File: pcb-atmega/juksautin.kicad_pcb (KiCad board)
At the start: 2 copper layers, 65 x 35 mm, 29 parts, among them J1 Screw_Terminal_01x09, J2 Power out, J3 USB_C_Receptacle_USB2.0, J4 TagConnect, J5 EXTRA, J6 AREF_OUT, U1 SP3485EN, U2 SRV05-4, U3 R-78E5.0-0.5, U4 ATmega32U4-AU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

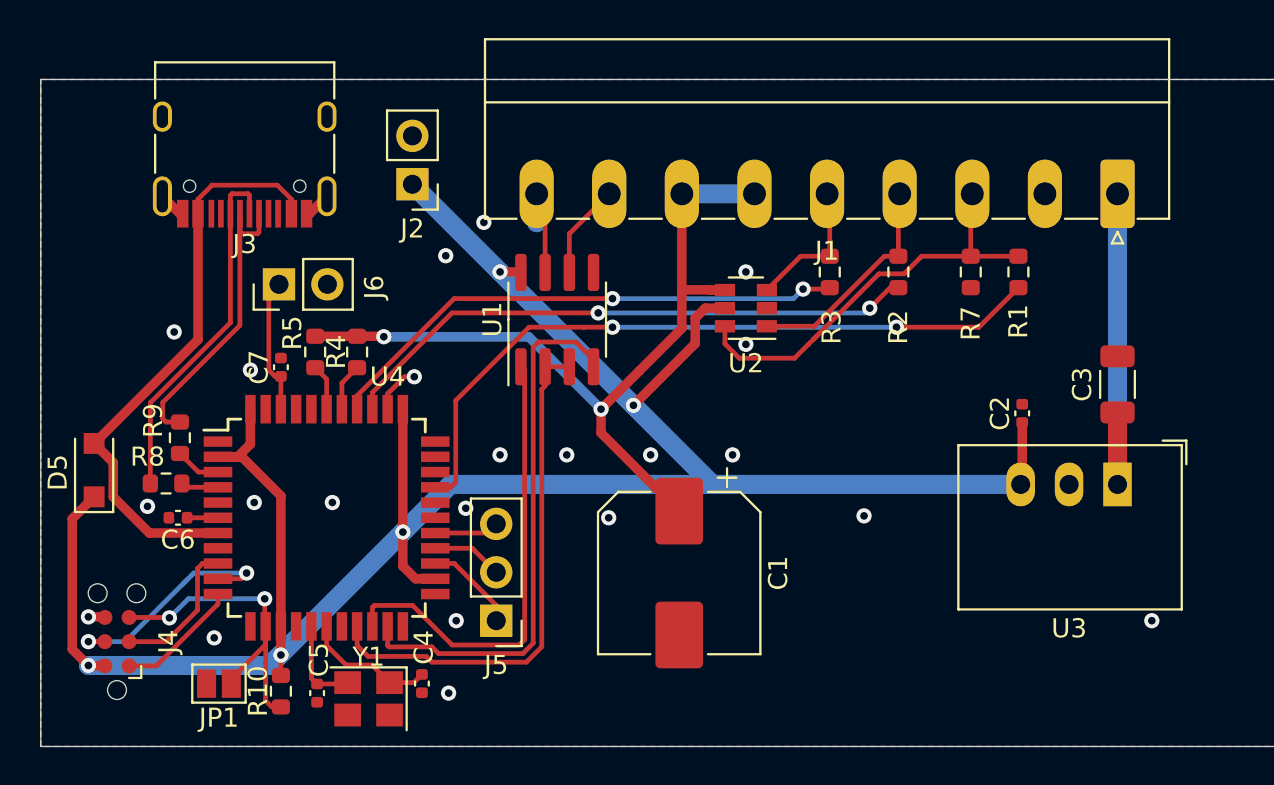
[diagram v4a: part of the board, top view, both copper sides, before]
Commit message: Atmega328 based pcb layed out
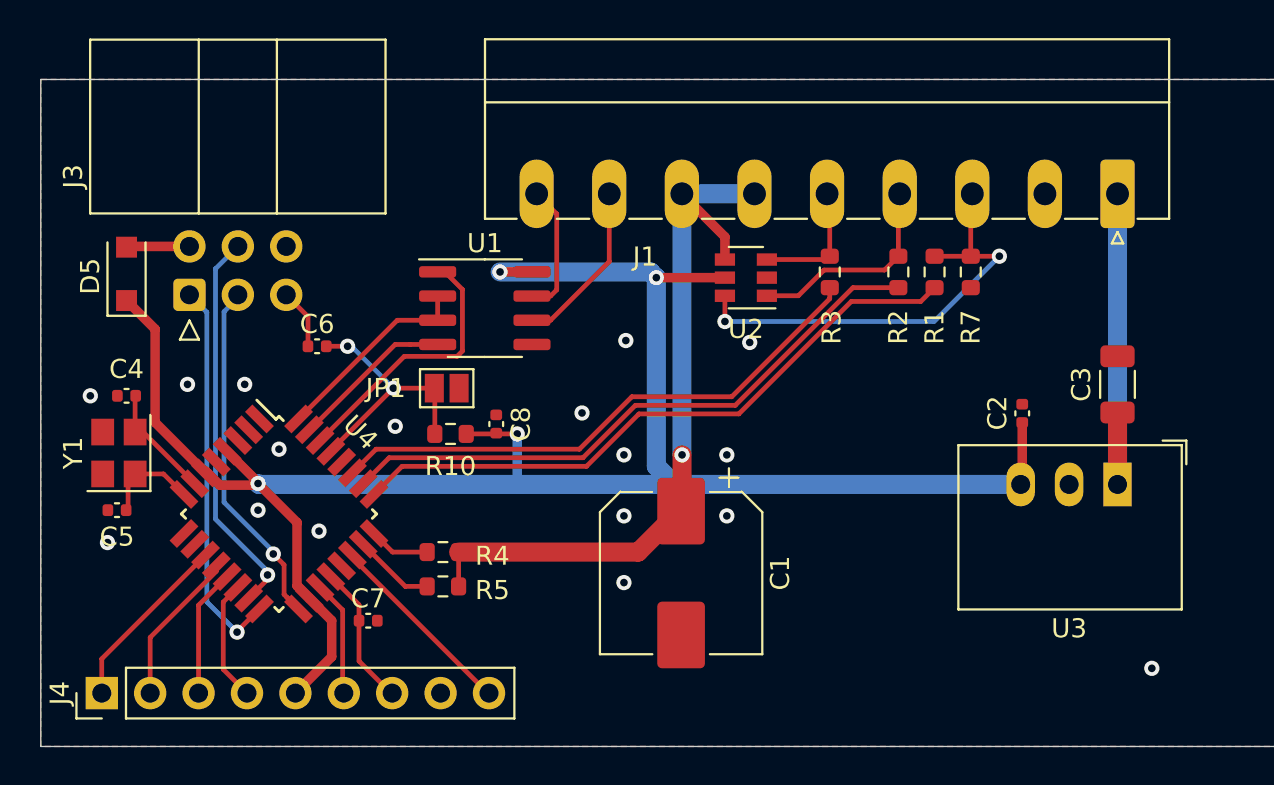
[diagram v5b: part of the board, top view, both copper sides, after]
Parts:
- removed J2: Power out, Connector_PinHeader_2.54mm:PinHeader_1x02_P2.54mm_Vertical
- removed J5: EXTRA, Connector_PinHeader_2.54mm:PinHeader_1x03_P2.54mm_Vertical
- removed J6: AREF_OUT, Connector_PinHeader_2.54mm:PinHeader_1x02_P2.54mm_Vertical
- removed R8, R9: 22, Resistor_SMD:R_0603_1608Metric
- added C8: 100n, Capacitor_SMD:C_0402_1005Metric, F.Cu at (133.9, 83.1)
- C6: value 1u -> 100n
- J3: value USB_C_Receptacle_USB2.0 -> AVR-ISP-6; footprint Connector_USB:USB_C_Receptacle_HRO_TYPE-C-31-M-12 -> Connector_IDC:IDC-Header_2x03_P2.54mm_Horizontal
- J4: value TagConnect -> Conn_01x09; footprint Connector:Tag-Connect_TC2030-IDC-NL_2x03_P1.27mm_Vertical -> Connector_PinHeader_2.54mm:PinHeader_1x09_P2.54mm_Vertical
- R10: value 20k -> 10k
- U4: value ATmega32U4-AU -> ATmega328P-AU; footprint Package_QFP:TQFP-44_10x10mm_P0.8mm -> Package_QFP:TQFP-32_7x7mm_P0.8mm
- moved C4 21.6 mm to (114.5, 81.6), turned to 180 degrees
- moved JP1 19.6 mm to (131.3, 81.2), turned to 0 degrees
- moved Y1 18.4 mm to (114.1, 84.6), turned to 90 degrees
- moved R10 16.2 mm to (131.5, 83.6), turned to 180 degrees
- moved C5 14.2 mm to (114.0, 87.6), turned to 180 degrees
- moved C7 14.1 mm to (127.2, 93.4), turned to 0 degrees
- moved R5 14.0 mm to (131.1, 91.6), turned to 0 degrees
- moved C6 11.6 mm to (124.5, 79.0), turned to 0 degrees
- moved R4 11.4 mm to (131.1, 89.8), turned to 0 degrees
- moved D5 10.4 mm to (114.5, 75.2)
- moved J3 8.79 mm to (117.8, 76.3), turned to 90 degrees
- moved R1 4.40 mm to (156.9, 75.1)
- moved U1 3.85 mm to (133.3, 77.0), turned to 0 degrees
- moved J4 2.82 mm to (113.2, 97.2)
- moved U4 2.51 mm to (122.5, 87.8), turned to 315 degrees
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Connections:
- C6 pad 1: Net-(C6-Pad1) -> /RESET_IN
- C6 pad 2: GND -> /RESET
- J4 pad 1: /MISO -> /INO_D7
- J4 pad 2: VCC -> /INO_D8
- J4 pad 3: /SCK -> /INO_D9
- J4 pad 4: /MOSI -> /INO_D10
- J4 pad 5: /RESET -> VCC
- J4 pad 6: GND -> /INO_A6
- U4 pad 10: /MOSI -> (no net)
- U4 pad 11: /MISO -> /INO_D7
- U4 pad 12: (no net) -> /INO_D8
- U4 pad 13: /RESET -> /INO_D9
- U4 pad 14: VCC -> /INO_D10
- U4 pad 15: GND -> /MOSI
- U4 pad 16: Net-(C5-Pad1) -> /MISO
- U4 pad 17: Net-(C4-Pad1) -> /SCK
- U4 pad 18: (no net) -> VCC
- U4 pad 19: /TX_EN -> /INO_A6
- U4 pad 2: VCC -> (no net)
- U4 pad 20: /RX -> /AREF
- U4 pad 21: /TX -> GND
- U4 pad 22: (no net) -> /INO_A7
- U4 pad 23: GND -> /FB
- U4 pad 24: VCC -> /DRIVE
- U4 pad 25: Net-(J5-Pad1) -> /PUMPFAIL_M
- U4 pad 26: Net-(J5-Pad2) -> /IO1_M
- U4 pad 27: Net-(J5-Pad3) -> /IO2_M
- U4 pad 29: (no net) -> /RESET
- U4 pad 3: /DM -> GND
- U4 pad 30: /PUMPFAIL_M -> /RX
- U4 pad 31: (no net) -> /TX
- U4 pad 32: (no net) -> /TX_EN
- U4 pad 4: /DP -> VCC
- U4 pad 6: Net-(C6-Pad1) -> VCC
- U4 pad 7: /VBUS -> Net-(C4-Pad1)
- U4 pad 8: (no net) -> Net-(C5-Pad1)
- U4 pad 9: /SCK -> (no net)
- Y1 pad 1: Net-(C4-Pad1) -> Net-(C5-Pad1)
- Y1 pad 2: Net-(C5-Pad1) -> Net-(C4-Pad1)
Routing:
- net VCC: track 141.8 -> 103.8 mm, vias 5 -> 4
- net /VBUS: track 30.8 -> 3.46 mm
- net /TX: track 28.6 -> 8.59 mm
- net Net-(J3-PadA6): track 18.9 -> 0.00 mm
- net /TX_EN: track 27.4 -> 10.7 mm
- net Net-(J3-PadA7): track 16.4 -> 0.00 mm
- net /MISO: track 6.53 -> 20.4 mm, vias 0 -> 1
- net /SCK: track 7.64 -> 19.3 mm, vias 0 -> 1
- net /INO_A7: track 0.00 -> 10.2 mm
- net /RX: track 24.4 -> 14.3 mm
- net /INO_D7: track 0.00 -> 9.50 mm
- net /INO_D8: track 0.00 -> 8.12 mm
- net /MOSI: track 12.7 -> 20.6 mm, vias 2 -> 1
- net /INO_D10: track 0.00 -> 7.11 mm
- net /INO_D9: track 0.00 -> 6.73 mm
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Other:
- board text added: "https://github.com/zouppen/pumpunjuksautin v0.9"
- board text removed: "v0.9 https://github.com/zouppen/pumpunjuksautin"

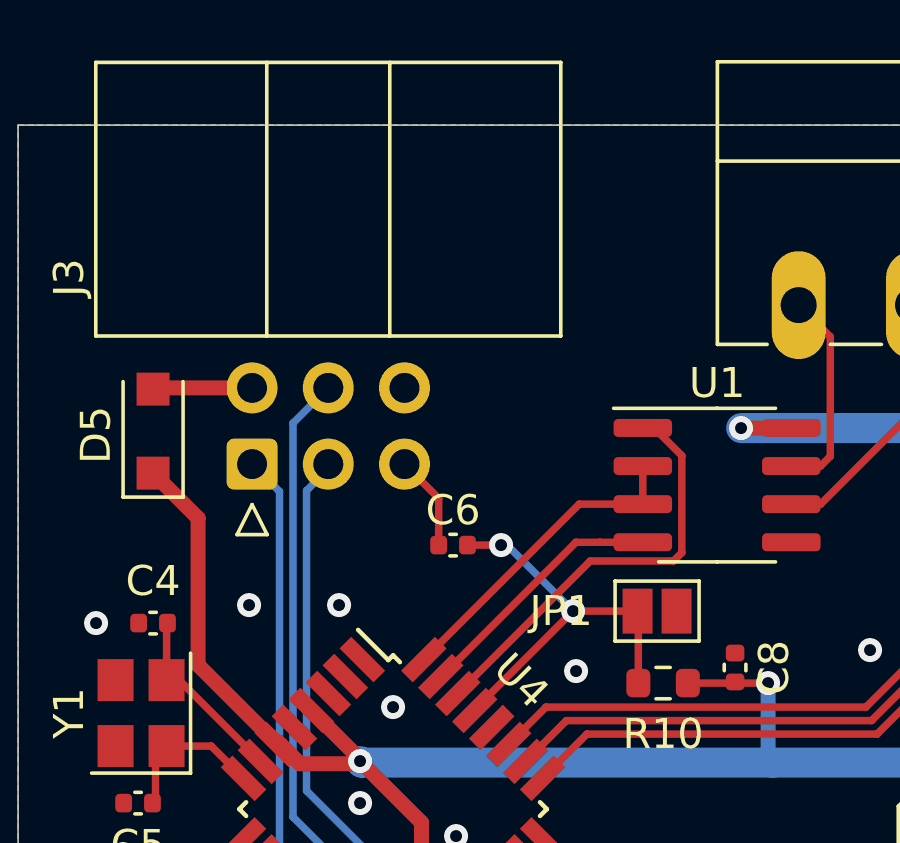
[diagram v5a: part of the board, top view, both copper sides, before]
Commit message: Add an indicator LED
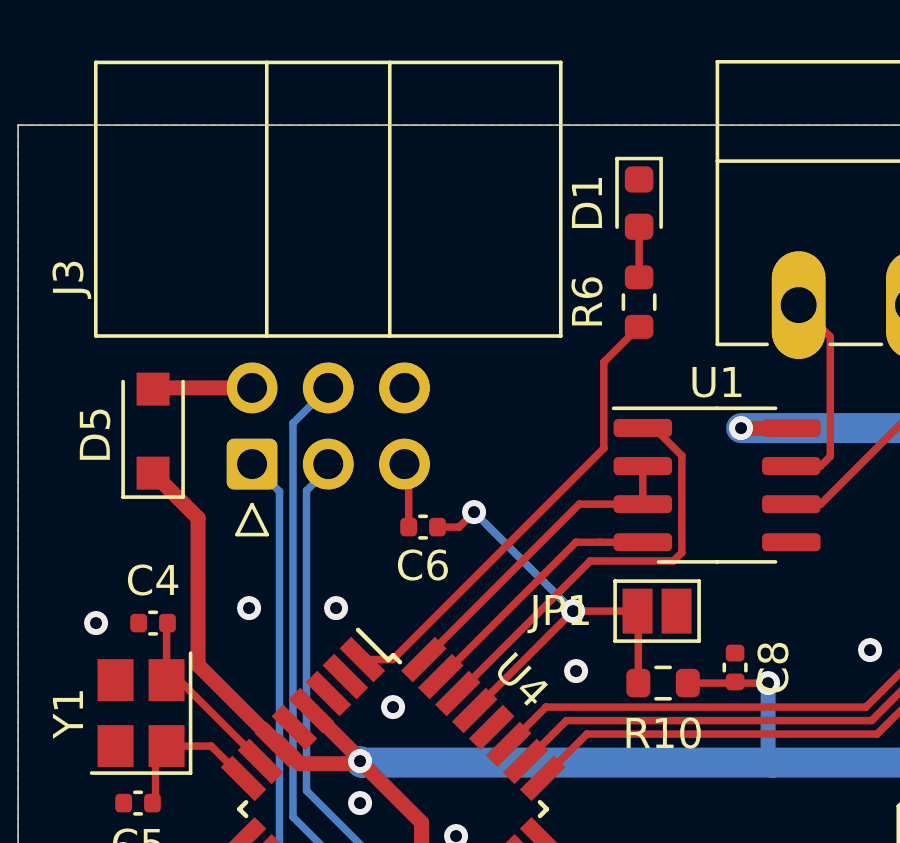
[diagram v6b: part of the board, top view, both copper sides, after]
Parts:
- added D1: LED, LED_SMD:LED_0603_1608Metric, F.Cu at (130.7, 67.6)
- added R6: 300, Resistor_SMD:R_0603_1608Metric, F.Cu at (130.7, 70.9)
- moved C6 1.17 mm to (123.5, 78.4)
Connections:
- U4 pad 1: (no net) -> Net-(R6-Pad2)
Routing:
- net Net-(R6-Pad2): track 0.00 -> 15.5 mm
- net /RESET: track 13.8 -> 19.5 mm
- net Net-(D1-Pad2): track 0.00 -> 1.69 mm
- net /RESET_IN: track 3.31 -> 2.30 mm

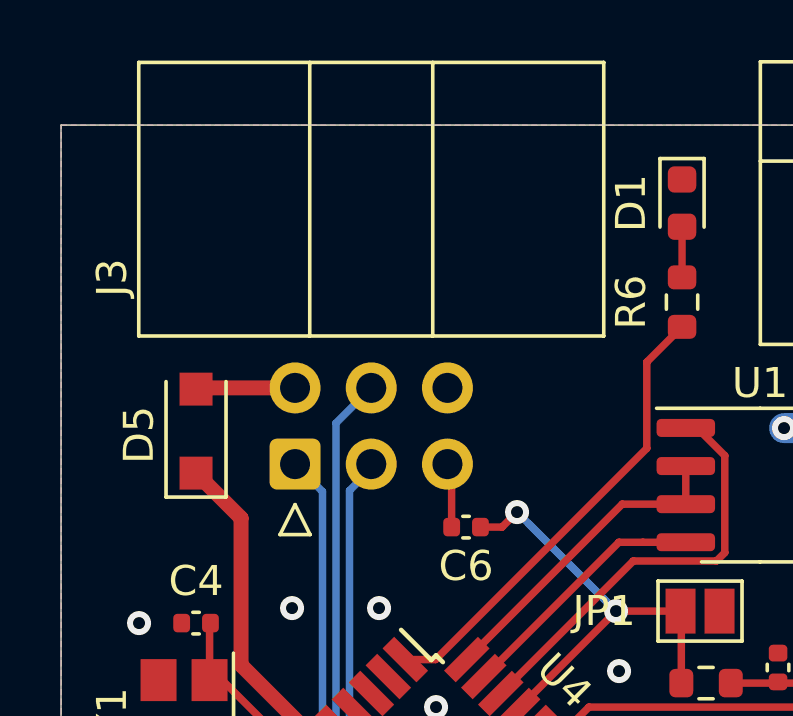
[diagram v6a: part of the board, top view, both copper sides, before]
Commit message: pcb: Replace IDC-6 connector with plain pins. The casing is 3D printed.
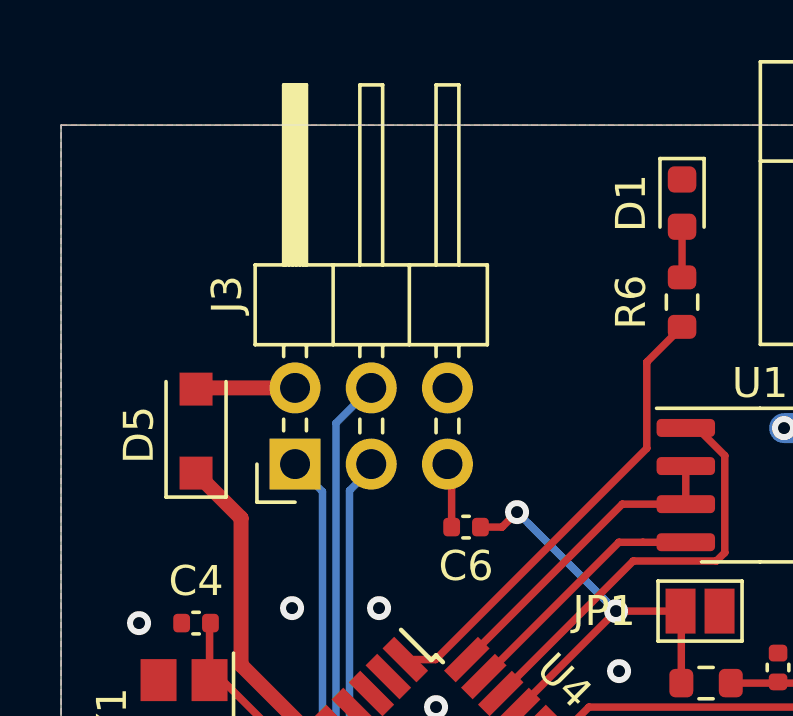
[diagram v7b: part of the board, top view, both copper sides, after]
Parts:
- J3: footprint Connector_IDC:IDC-Header_2x03_P2.54mm_Horizontal -> Connector_PinHeader_2.54mm:PinHeader_2x03_P2.54mm_Horizontal
- JP1: value SolderJumper_2_Open -> Reset pad

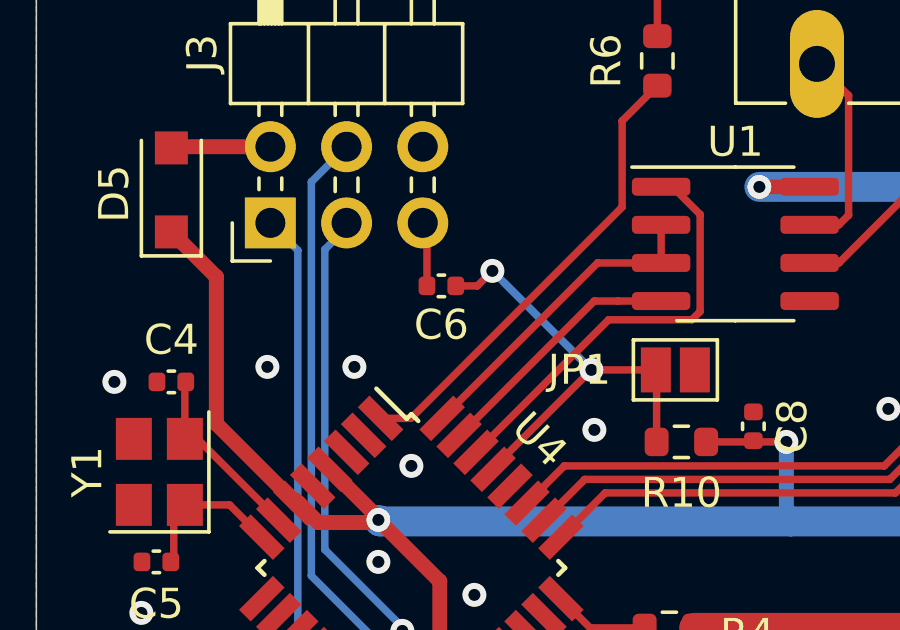
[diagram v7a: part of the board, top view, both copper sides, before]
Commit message: pcb: Make it pass DRC test (clean courtyards
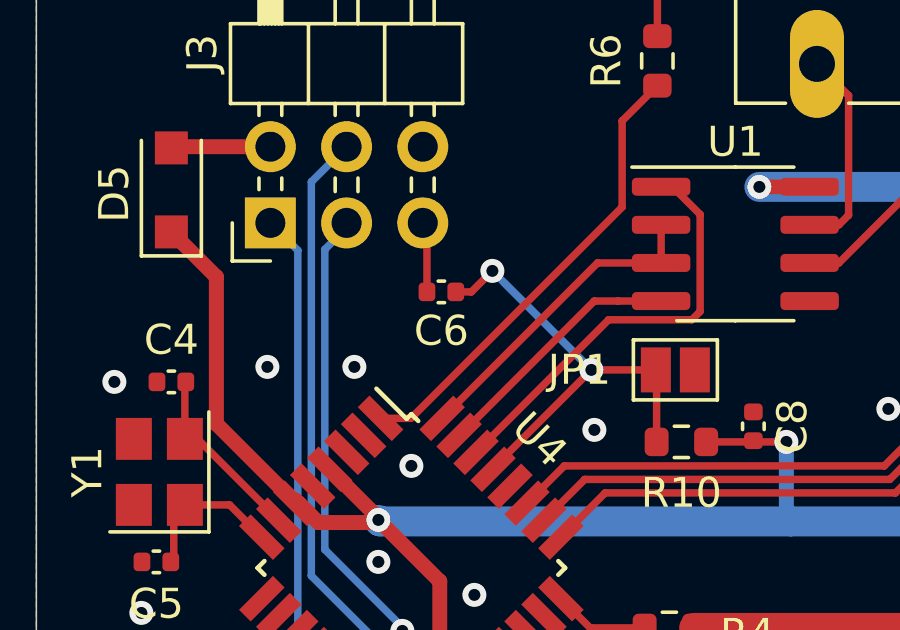
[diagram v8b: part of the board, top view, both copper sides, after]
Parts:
- moved C6 0.20 mm to (123.5, 78.6)
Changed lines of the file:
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@@
     (add_net "Net-(D1-Pad2)")
     (add_net "Net-(R6-Pad2)")
-    (add_net "Net-(U4-Pad10)")
-    (add_net "Net-(U4-Pad2)")
-    (add_net "Net-(U4-Pad28)")
-    (add_net "Net-(U4-Pad9)")
     (add_net PUMPFAIL)
     (add_net VCC)
@@
   )
   (module Capacitor_SMD:C_0402_1005Metric (layer F.Cu)
-    (at 123.5 78.4)
+    (at 123.5 78.6)
     (descr "Capacitor SMD 0402 (1005 Metric), square (rectangular) end terminal, IPC_7351 nominal, (Body size source: IPC-SM-782 page 76, https://www.pcb-3d.com/wordpress/wp-content/uploads/ipc-sm-782a_amendment_1_and_2.pdf), generated with kicad-footprint-generator")
     (tags capacitor)
@@
   (segment (start 128.5 81.2) (end 130.65 81.2) (width 0.25) (layer F.Cu) (net 13))
   (segment (start 125.222361 84.477639) (end 128.5 81.2) (width 0.25) (layer F.Cu) (net 13))
-  (via (at 125.2 77.9) (size 0.8) (drill 0.4) (layers F.Cu B.Cu) (net 13))
   (via (at 128.5 81.2) (size 0.8) (drill 0.4) (layers F.Cu B.Cu) (net 13))
   (segment (start 128.4 81.2) (end 128.5 81.2) (width 0.25) (layer B.Cu) (net 13))
   (segment (start 125.6 78.3) (end 128.5 81.2) (width 0.25) (layer B.Cu) (net 13))
+  (via (at 125.2 77.9) (size 0.8) (drill 0.4) (layers F.Cu B.Cu) (net 13))
   (segment (start 125.2 77.9) (end 128.5 81.2) (width 0.25) (layer B.Cu) (net 13))
-  (segment (start 124.7 78.4) (end 125.2 77.9) (width 0.25) (layer F.Cu) (net 13))
-  (segment (start 123.98 78.4) (end 124.7 78.4) (width 0.25) (layer F.Cu) (net 13))
+  (segment (start 124.5 78.6) (end 125.2 77.9) (width 0.25) (layer F.Cu) (net 13))
+  (segment (start 123.98 78.6) (end 124.5 78.6) (width 0.25) (layer F.Cu) (net 13))
   (segment (start 121.9 91.228427) (end 121.9 90.8) (width 0.25) (layer F.Cu) (net 14))
   (segment (start 120.90901 92.219417) (end 121.9 91.228427) (width 0.25) (layer F.Cu) (net 14))
